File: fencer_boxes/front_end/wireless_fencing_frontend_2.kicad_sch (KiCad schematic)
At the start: 18 parts, among them J1 Conn_01x03, J2 Conn_01x08, U2 AD8619

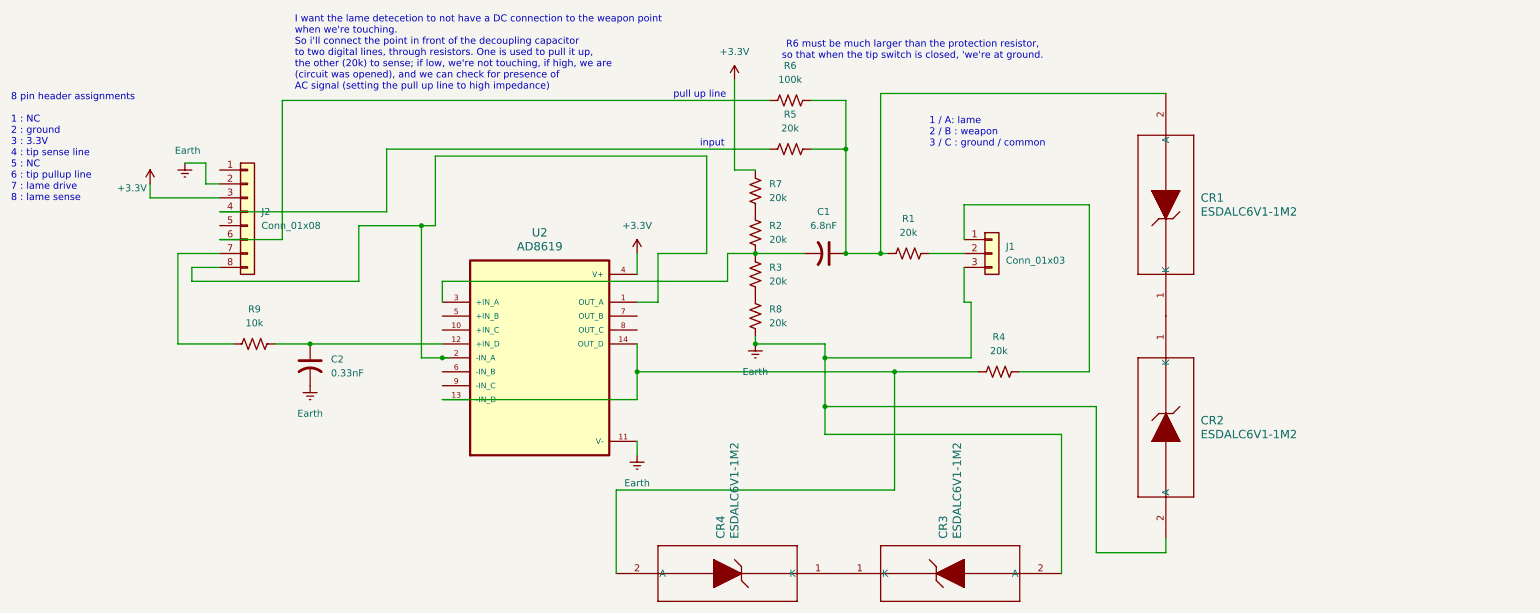
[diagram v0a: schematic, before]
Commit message: front end tvs and resistor combination
* Single SOD-523 footprint for TVS diodes
* Changed from using 2x20kOhm in series to single 40kOhm.
Initially was trying to minimize the number of different values, but resistors
are like a cent a piece, even in pretty small quantities, and this saves soldering.
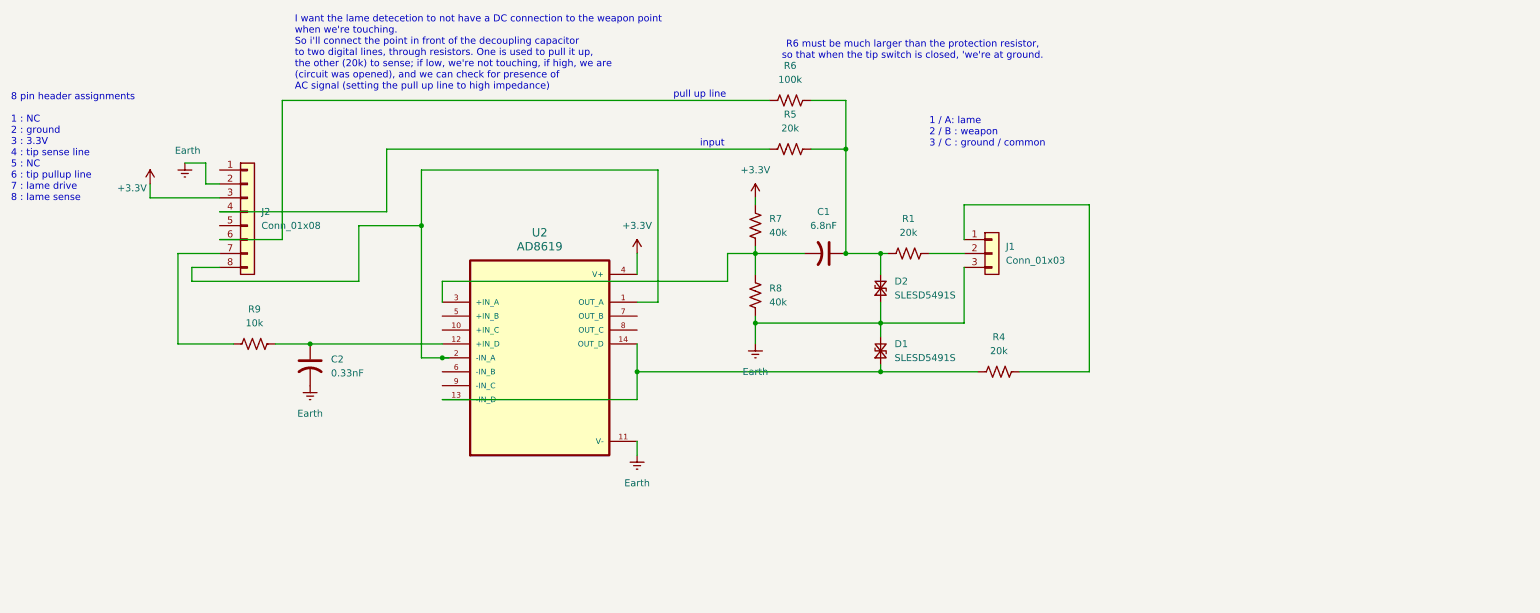
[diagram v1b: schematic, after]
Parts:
- removed CR1, CR2, CR3, CR4: ESDALC6V1-1M2, ESDALC6V1:SOD882_STM, symbol 2025-12-14_07-55-12:ESDALC6V1-1M2
- removed R2, R3: 20k, Resistor_SMD:R_0805_2012Metric, symbol Device:R_US
- added D1, D2: SLESD5491S, Diode_SMD:D_SOD-523, symbol Device:D_TVS_Small
- R7, R8: value 20k -> 40k
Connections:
- net Earth: now also D1.2 (A2), D2.1 (A1)
- net at R8.2: now also C1.2, R7.1, U2.3 (+IN_A)
- net at C1.1, R1.1, R5.2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: now also D2.2 (A2)
- net at R4.1, U2.13 (-IN_D), U2.14 (OUT_D): now also D1.1 (A1)
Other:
- moved on the sheet: R7, R8

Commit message: Adding simple passive lowpass before  adc buffer
set to 10k, 1nF i.e. f0 16kHz ; used 11k, not critical.

i've bodged this into the existing boards.
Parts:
- added C3: 1nF, Capacitor_SMD:C_0805_2012Metric, symbol Device:C_US
- added R2: 10k, Resistor_SMD:R_0805_2012Metric, symbol Device:R_US
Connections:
- net Earth: now also C3.2
- net at C1.2, R7.1, R8.2: now also R2.1; no longer U2.3 (+IN_A)
- new net: C3.1, R2.2, U2.3 (+IN_A)
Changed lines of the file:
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@@
 		(color 0 0 0 0)
 	)
+	(junction
+		(at 176.53 101.6)
+		(diameter 0)
+		(color 0 0 0 0)
+	)
 	(wire
 		(pts
@@
 	(wire
 		(pts
+			(xy 132.08 91.44) (xy 132.08 110.49)
+		)
+		(stroke
+			(width 0)
+			(type default)
+		)
+	)
+	(wire
+		(pts
 			(xy 121.92 93.98) (xy 121.92 82.55)
 		)
@@
 	(wire
 		(pts
-			(xy 132.08 106.68) (xy 184.15 106.68)
-		)
-		(stroke
-			(width 0)
-			(type default)
-		)
-	)
-	(wire
-		(pts
 			(xy 107.95 118.11) (xy 132.08 118.11)
 		)
@@
 	(wire
 		(pts
-			(xy 184.15 106.68) (xy 184.15 101.6)
-		)
-		(stroke
-			(width 0)
-			(type default)
-		)
-	)
-	(wire
-		(pts
 			(xy 167.64 118.11) (xy 167.64 123.19)
 		)
@@
 	(wire
 		(pts
-			(xy 132.08 110.49) (xy 132.08 106.68)
-		)
-		(stroke
-			(width 0)
-			(type default)
-		)
-	)
-	(wire
-		(pts
 			(xy 205.74 73.66) (xy 205.74 82.55)
 		)
@@
 	(wire
 		(pts
+			(xy 176.53 114.3) (xy 189.23 114.3)
+		)
+		(stroke
+			(width 0)
+			(type default)
+		)
+	)
+	(wire
+		(pts
+			(xy 176.53 109.22) (xy 176.53 114.3)
+		)
+		(stroke
+			(width 0)
+			(type default)
+		)
+	)
+	(wire
+		(pts
 			(xy 86.36 106.68) (xy 116.84 106.68)
 		)
@@
 	(wire
 		(pts
+			(xy 176.53 101.6) (xy 176.53 91.44)
+		)
+		(stroke
+			(width 0)
+			(type default)
+		)
+	)
+	(wire
+		(pts
 			(xy 128.27 86.36) (xy 128.27 96.52)
 		)
@@
 		(pts
 			(xy 205.74 82.55) (xy 199.39 82.55)
+		)
+		(stroke
+			(width 0)
+			(type default)
+		)
+	)
+	(wire
+		(pts
+			(xy 176.53 91.44) (xy 132.08 91.44)
 		)
 		(stroke
@@
 	)
 	(symbol
+		(lib_id "Device:C_US")
+		(at 176.53 105.41 0)
+		(unit 1)
+		(exclude_from_sim no)
+		(in_bom yes)
+		(on_board yes)
+		(dnp no)
+		(fields_autoplaced yes)
+		(property "Reference" "C3"
+			(at 180.34 104.3939 0)
+			(effects
+				(font
+					(size 1.27 1.27)
+				)
+				(justify left)
+			)
+		)
+		(property "Value" "1nF"
+			(at 180.34 106.9339 0)
+			(effects
+				(font
+					(size 1.27 1.27)
+				)
+				(justify left)
+			)
+		)
+		(property "Footprint" "Capacitor_SMD:C_0805_2012Metric"
+			(at 176.53 105.41 0)
+			(effects
+				(font
+					(size 1.27 1.27)
+				)
+				(hide yes)
+			)
+		)
+		(property "Datasheet" ""
+			(at 176.53 105.41 0)
+			(effects
+				(font
+					(size 1.27 1.27)
+				)
+				(hide yes)
+			)
+		)
+		(property "Description" "capacitor, US symbol"
+			(at 176.53 105.41 0)
+			(effects
+				(font
+					(size 1.27 1.27)
+				)
+				(hide yes)
+			)
+		)
+		(pin "2"
+		)
+		(pin "1"
+		)
+		(instances
+			(project "wireless_fencing_frontend_2"
+				(path "/68d4213b-91f0-4b51-a69b-1e4a432a965b"
+					(reference "C3")
+					(unit 1)
+				)
+			)
+		)
+	)
+	(symbol
 		(lib_id "Device:R_US")
 		(at 97.79 118.11 90)
@@
 					(unit 1)
 				)
+			)
+		)
+	)
+	(symbol
+		(lib_id "Device:R_US")
+		(at 180.34 101.6 270)
+		(unit 1)
+		(exclude_from_sim no)
+		(in_bom yes)
+		(on_board yes)
+		(dnp no)
+		(fields_autoplaced yes)
+		(property "Reference" "R2"
+			(at 180.34 95.25 90)
+			(effects
+				(font
+					(size 1.27 1.27)
+				)
+			)
+		)
+		(property "Value" "10k"
+			(at 180.34 97.79 90)
+			(effects
+				(font
+					(size 1.27 1.27)
+				)
+			)
+		)
+		(property "Footprint" "Resistor_SMD:R_0805_2012Metric"
+			(at 180.086 102.616 90)
+			(effects
+				(font
+					(size 1.27 1.27)
+				)
+				(hide yes)
+			)
+		)
+		(property "Datasheet" "~"
+			(at 180.34 101.6 0)
+			(effects
+				(font
+					(size 1.27 1.27)
+				)
+				(hide yes)
+			)
+		)
+		(property "Description" "Resistor, US symbol"
+			(at 180.34 101.6 0)
+			(effects
+				(font
+					(size 1.27 1.27)
+				)
+				(hide yes)
+			)
+		)
+		(pin "2"
+		)
+		(pin "1"
+		)
+		(instances
+			(project "wireless_fencing_frontend_2"
+				(path "/68d4213b-91f0-4b51-a69b-1e4a432a965b"
+					(reference "R2")
+					(unit 1)
+				)

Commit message: lame drive changed from 20k to 2k
just matching change in reality; not sure if it's important.
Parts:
- R4: value 20k -> 2k
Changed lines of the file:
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@@
 			)
 		)
-		(property "Value" "20k"
+		(property "Value" "2k"
 			(at 233.68 119.38 90)
 			(effects

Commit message: Adding lame pulldown and common line to ground resistor
so now the lame connection is
1. on a voltage divider between the drive and ground, not floating.
2. setting this to 100 ohm drive, 200 ohm to ground - so also much stronger than before.
and the C (common) line is not tied directly to ground, but has a 2k resistor.

Overall, this doesn't change the tip detection much, but should make the lame drive more
resistant to the common line touching the lame (cause of e.g. sweaty skin). Before this
changed it from floating to grounded, now it 1. does not connect it directly to ground,
but only through a 2k resistor, and 2. the drive is much stronger and more deterministic,
so this won't change the bias much.
It does mean we're consuming about 15mW more (3.3 V over 300 ohm, at 50% duty cycle)
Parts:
- added R10: 200, Resistor_SMD:R_0805_2012Metric, symbol Device:R_US
- added R3: 2k, Resistor_SMD:R_0805_2012Metric, symbol Device:R_US
- R4: value 2k -> 100
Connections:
- net Earth: now also R10.1, R3.1; no longer J1.3 (Pin_3)
- net at J1.1 (Pin_1), R4.2: now also R10.2
- new net: J1.3 (Pin_3), R3.2
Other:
- note added: "R6 must be much larger than the protection resistor + common to ground resistor so that when the tip switch is closed, 'we're at ground."
- note added: "adding a pulldown to the lame line. would make voltage more deterministic. needs to be small enough that a lame to weapon common short is not a problem. note: this will be a significant draw - e.g. 300 ohm is 10mA (30mW), but not dominant vs e.g. pico2w"
- note removed: "R6 must be much larger than the protection resistor, so that when the tip switch is closed, 'we're at ground."
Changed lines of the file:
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@@
 		)
 	)
-	(text "R6 must be much larger than the protection resistor,\nso that when the tip switch is closed, 'we're at ground."
+	(text "R6 must be much larger than the protection resistor + common to ground resistor\nso that when the tip switch is closed, 'we're at ground."
 		(exclude_from_sim no)
 		(at 217.932 64.516 0)
@@
 		)
 	)
+	(text "adding a pulldown to the lame line.\nwould make voltage more deterministic.\nneeds to be small enough that a lame to weapon common\n  short is not a problem.\nnote: this will be a significant draw - e.g. 300 ohm\nis 10mA (30mW), but not dominant vs e.g. pico2w"
+		(exclude_from_sim no)
+		(at 209.042 141.478 0)
+		(effects
+			(font
+				(size 1.27 1.27)
+			)
+			(justify left)
+		)
+	)
 	(text "I want the lame detecetion to not have a DC connection to the weapon point\nwhen we're touching.\nSo i'll connect the point in front of the decoupling capacitor\nto two digital lines, through resistors. One is used to pull it up,\nthe other (20k) to sense; if low, we're not touching, if high, we are\n(circuit was opened), and we can check for presence of\nAC signal (setting the pull up line to high impedance)"
 		(exclude_from_sim no)
@@
 	)
 	(junction
+		(at 250.19 123.19)
+		(diameter 0)
+		(color 0 0 0 0)
+	)
+	(junction
 		(at 212.09 114.3)
 		(diameter 0)
@@
 	(wire
 		(pts
+			(xy 223.52 114.3) (xy 227.33 114.3)
+		)
+		(stroke
+			(width 0)
+			(type default)
+		)
+	)
+	(wire
+		(pts
 			(xy 212.09 121.92) (xy 212.09 123.19)
 		)
@@
 	(wire
 		(pts
-			(xy 212.09 114.3) (xy 227.33 114.3)
+			(xy 212.09 114.3) (xy 215.9 114.3)
 		)
 		(stroke
@@
 	)
 	(symbol
+		(lib_id "Device:R_US")
+		(at 250.19 127 180)
+		(unit 1)
+		(exclude_from_sim no)
+		(in_bom yes)
+		(on_board yes)
+		(dnp no)
+		(fields_autoplaced yes)
+		(property "Reference" "R10"
+			(at 252.73 125.7299 0)
+			(effects
+				(font
+					(size 1.27 1.27)
+				)
+				(justify right)
+			)
+		)
+		(property "Value" "200"
+			(at 252.73 128.2699 0)
+			(effects
+				(font
+					(size 1.27 1.27)
+				)
+				(justify right)
+			)
+		)
+		(property "Footprint" "Resistor_SMD:R_0805_2012Metric"
+			(at 249.174 126.746 90)
+			(effects
+				(font
+					(size 1.27 1.27)
+				)
+				(hide yes)
+			)
+		)
+		(property "Datasheet" "~"
+			(at 250.19 127 0)
+			(effects
+				(font
+					(size 1.27 1.27)
+				)
+				(hide yes)
+			)
+		)
+		(property "Description" "Resistor, US symbol"
+			(at 250.19 127 0)
+			(effects
+				(font
+					(size 1.27 1.27)
+				)
+				(hide yes)
+			)
+		)
+		(pin "1"
+		)
+		(pin "2"
+		)
+		(instances
+			(project "wireless_fencing_frontend_2"
+				(path "/68d4213b-91f0-4b51-a69b-1e4a432a965b"
+					(reference "R10")
+					(unit 1)
+				)
+			)
+		)
+	)
+	(symbol
 		(lib_id "Connector_Generic:Conn_01x08")
 		(at 96.52 93.98 0)
@@
 	)
 	(symbol
+		(lib_id "Device:R_US")
+		(at 219.71 114.3 90)
+		(unit 1)
+		(exclude_from_sim no)
+		(in_bom yes)
+		(on_board yes)
+		(dnp no)
+		(fields_autoplaced yes)
+		(property "Reference" "R3"
+			(at 219.71 107.95 90)
+			(effects
+				(font
+					(size 1.27 1.27)
+				)
+			)
+		)
+		(property "Value" "2k"
+			(at 219.71 110.49 90)
+			(effects
+				(font
+					(size 1.27 1.27)
+				)
+			)
+		)
+		(property "Footprint" "Resistor_SMD:R_0805_2012Metric"
+			(at 219.964 113.284 90)
+			(effects
+				(font
+					(size 1.27 1.27)
+				)
+				(hide yes)
+			)
+		)
+		(property "Datasheet" "~"
+			(at 219.71 114.3 0)
+			(effects
+				(font
+					(size 1.27 1.27)
+				)
+				(hide yes)
+			)
+		)
+		(property "Description" "Resistor, US symbol"
+			(at 219.71 114.3 0)
+			(effects
+				(font
+					(size 1.27 1.27)
+				)
+				(hide yes)
+			)
+		)
+		(pin "2"
+		)
+		(pin "1"
+		)
+		(instances
+			(project "wireless_fencing_frontend_2"
+				(path "/68d4213b-91f0-4b51-a69b-1e4a432a965b"
+					(reference "R3")
+					(unit 1)
+				)
+			)
+		)
+	)
+	(symbol
+		(lib_id "power:Earth")
+		(at 250.19 130.81 0)
+		(unit 1)
+		(exclude_from_sim no)
+		(in_bom yes)
+		(on_board yes)
+		(dnp no)
+		(fields_autoplaced yes)
+		(property "Reference" "#PWR03"
+			(at 250.19 137.16 0)
+			(effects
+				(font
+					(size 1.27 1.27)
+				)
+				(hide yes)
+			)
+		)
+		(property "Value" "Earth"
+			(at 250.19 135.89 0)
+			(effects
+				(font
+					(size 1.27 1.27)
+				)
+			)
+		)
+		(property "Footprint" ""
+			(at 250.19 130.81 0)
+			(effects
+				(font
+					(size 1.27 1.27)
+				)
+				(hide yes)
+			)
+		)
+		(property "Datasheet" "~"
+			(at 250.19 130.81 0)
+			(effects
+				(font
+					(size 1.27 1.27)
+				)
+				(hide yes)
+			)
+		)
+		(property "Description" "Power symbol creates a global label with name \"Earth\""
+			(at 250.19 130.81 0)
+			(effects
+				(font
+					(size 1.27 1.27)
+				)
+				(hide yes)
+			)
+		)
+		(pin "1"
+		)
+		(instances
+			(project "wireless_fencing_frontend_2"
+				(path "/68d4213b-91f0-4b51-a69b-1e4a432a965b"
+					(reference "#PWR03")
+					(unit 1)
+				)
+			)
+		)
+	)
+	(symbol
 		(lib_id "Device:D_TVS_Small")
 		(at 212.09 107.95 90)
@@
 		(on_board yes)
 		(dnp no)
-		(fields_autoplaced yes)
 		(property "Reference" "D2"
 			(at 214.63 106.6799 90)
@@
 		)
 		(property "Value" "SLESD5491S"
-			(at 214.63 109.2199 90)
+			(at 198.882 110.744 90)
 			(effects
 				(font
@@
 			)
 		)
-		(property "Value" "2k"
+		(property "Value" "100"
 			(at 233.68 119.38 90)
 			(effects

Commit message: Change to AC coupling of drive to lame
i.e. add a capacitor on the line.
with the recent addition of tying the lame drive to ground, if one
foil touches the opposite lame, the moment the other touch happens -
 - even before the switch is actually depressed - the voltage at the
pin can be back driven by the (opposite) lame and trigger a false touch.
Braking the DC coupling solves it.
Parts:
- added C4: 100nF, Capacitor_SMD:C_0805_2012Metric, symbol Device:C_US
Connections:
- net at R10.2, R4.2: now also C4.2; no longer J1.1 (Pin_1)
- new net: C4.1, J1.1 (Pin_1)
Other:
- note added: "capacitor to break DC connection - otherwise, if the tow foils touch the oppsite lames at the same time, the drive on the lames can backdrive the tip test point, and lead to a false indication of tip closure."
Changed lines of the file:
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@@
 	(text "adding a pulldown to the lame line.\nwould make voltage more deterministic.\nneeds to be small enough that a lame to weapon common\n  short is not a problem.\nnote: this will be a significant draw - e.g. 300 ohm\nis 10mA (30mW), but not dominant vs e.g. pico2w"
 		(exclude_from_sim no)
-		(at 209.042 141.478 0)
+		(at 259.08 129.286 0)
+		(effects
+			(font
+				(size 1.27 1.27)
+			)
+			(justify left)
+		)
+	)
+	(text "capacitor to break DC connection - otherwise,\nif the tow foils touch the oppsite lames at the same time,\nthe drive on the lames can backdrive the tip test point, and lead\nto a false indication of tip closure."
+		(exclude_from_sim no)
+		(at 251.714 101.346 0)
 		(effects
 			(font
@@
 	(wire
 		(pts
+			(xy 250.19 114.3) (xy 250.19 123.19)
+		)
+		(stroke
+			(width 0)
+			(type default)
+		)
+	)
+	(wire
+		(pts
 			(xy 205.74 101.6) (xy 212.09 101.6)
 		)
@@
 	(wire
 		(pts
-			(xy 250.19 92.71) (xy 250.19 123.19)
+			(xy 250.19 92.71) (xy 250.19 106.68)
 		)
 		(stroke
@@
 					(unit 1)
 				)
+			)
+		)
+	)
+	(symbol
+		(lib_id "Device:C_US")
+		(at 250.19 110.49 0)
+		(unit 1)
+		(exclude_from_sim no)
+		(in_bom yes)
+		(on_board yes)
+		(dnp no)
+		(fields_autoplaced yes)
+		(property "Reference" "C4"
+			(at 254 109.4739 0)
+			(effects
+				(font
+					(size 1.27 1.27)
+				)
+				(justify left)
+			)
+		)
+		(property "Value" "100nF"
+			(at 254 112.0139 0)
+			(effects
+				(font
+					(size 1.27 1.27)
+				)
+				(justify left)
+			)
+		)
+		(property "Footprint" "Capacitor_SMD:C_0805_2012Metric"
+			(at 250.19 110.49 0)
+			(effects
+				(font
+					(size 1.27 1.27)
+				)
+				(hide yes)
+			)
+		)
+		(property "Datasheet" ""
+			(at 250.19 110.49 0)
+			(effects
+				(font
+					(size 1.27 1.27)
+				)
+				(hide yes)
+			)
+		)
+		(property "Description" "capacitor, US symbol"
+			(at 250.19 110.49 0)
+			(effects
+				(font
+					(size 1.27 1.27)
+				)
+				(hide yes)
+			)
+		)
+		(pin "2"
+		)
+		(pin "1"
+		)
+		(instances
+			(project "wireless_fencing_frontend_2"
+				(path "/68d4213b-91f0-4b51-a69b-1e4a432a965b"
+					(reference "C4")
+					(unit 1)
+				)

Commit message: Adjusting lame drive hardware for a stronger drive
* reduce (well, eliminate) the inline resistance (i think not needed
once we're capacitively coupled to the lame)
* increase the capacitor from 100nF to 10uF.

Both of these changes seem to do better when the lame is "shorted" to
the common line; the current configs seem to do ok down to about 5kOhm
of a short, but no lower - so a super sweaty fencer is still an issue,
i think.
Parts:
- C4: value 100nF -> 10uF
- R4: value 100 -> 0
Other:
- note added: "adding a pulldown to the lame line. would make voltage more deterministic. needs to be small enough that a lame to weapon common short is not a problem. note: this will be a significant draw - e.g. 300 ohm is 10mA (30mW), but not dominant vs e.g. pico2w further reducing this to be the only load, so more extreme."
- note removed: "adding a pulldown to the lame line. would make voltage more deterministic. needs to be small enough that a lame to weapon common short is not a problem. note: this will be a significant draw - e.g. 300 ohm is 10mA (30mW), but not dominant vs e.g. pico2w"
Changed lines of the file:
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@@
 		)
 	)
-	(text "adding a pulldown to the lame line.\nwould make voltage more deterministic.\nneeds to be small enough that a lame to weapon common\n  short is not a problem.\nnote: this will be a significant draw - e.g. 300 ohm\nis 10mA (30mW), but not dominant vs e.g. pico2w"
+	(text "adding a pulldown to the lame line.\nwould make voltage more deterministic.\nneeds to be small enough that a lame to weapon common\n  short is not a problem.\nnote: this will be a significant draw - e.g. 300 ohm\nis 10mA (30mW), but not dominant vs e.g. pico2w\nfurther reducing this to be the only load, so more extreme."
 		(exclude_from_sim no)
 		(at 259.08 129.286 0)
@@
 		(on_board yes)
 		(dnp no)
-		(fields_autoplaced yes)
 		(property "Reference" "R10"
 			(at 252.73 125.7299 0)
@@
 			)
 		)
-		(property "Value" "100nF"
+		(property "Value" "10uF"
 			(at 254 112.0139 0)
 			(effects
@@
 			)
 		)
-		(property "Value" "100"
+		(property "Value" "0"
 			(at 233.68 119.38 90)
 			(effects
